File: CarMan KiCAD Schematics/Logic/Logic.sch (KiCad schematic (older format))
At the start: 48 parts, among them J1 Motor Controller Can Line, J2 NON-ISO I2C Testing Header, J3 Logic-TSI Connector, J4 GLV BOB, J5 PIC program, J6 You're Welcome -Ethan, J666 Real Time Clock, U1 MCP9700AT-HTT-Sensor_Temperat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, U10 BNO_055, U3 PIC32MZ2048EFM064-I_PT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

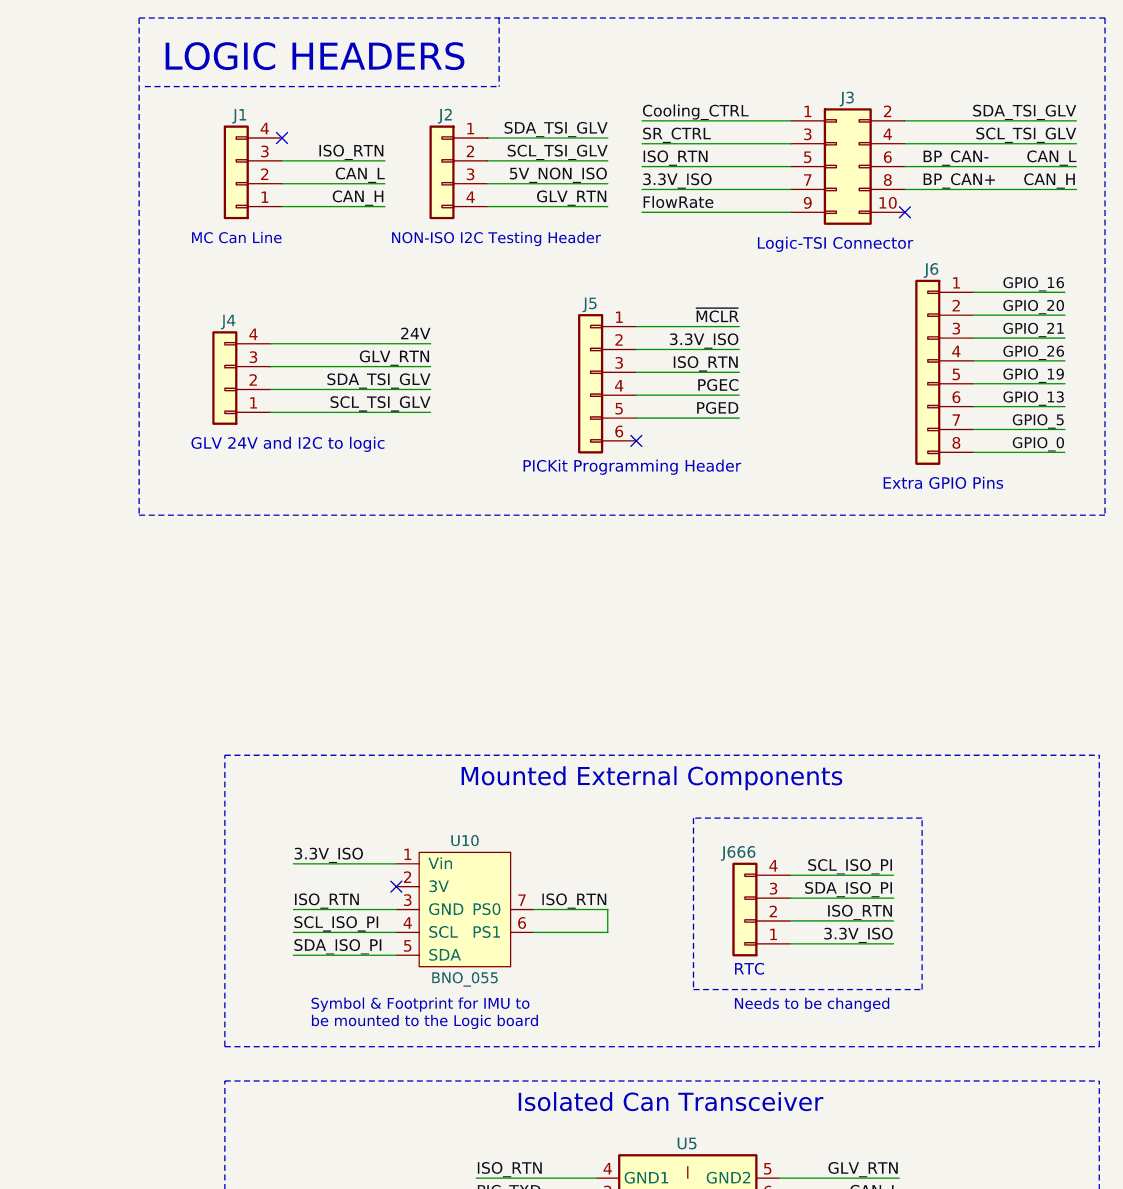
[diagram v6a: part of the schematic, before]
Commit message: Added Footprint for Pi RTC. organized board
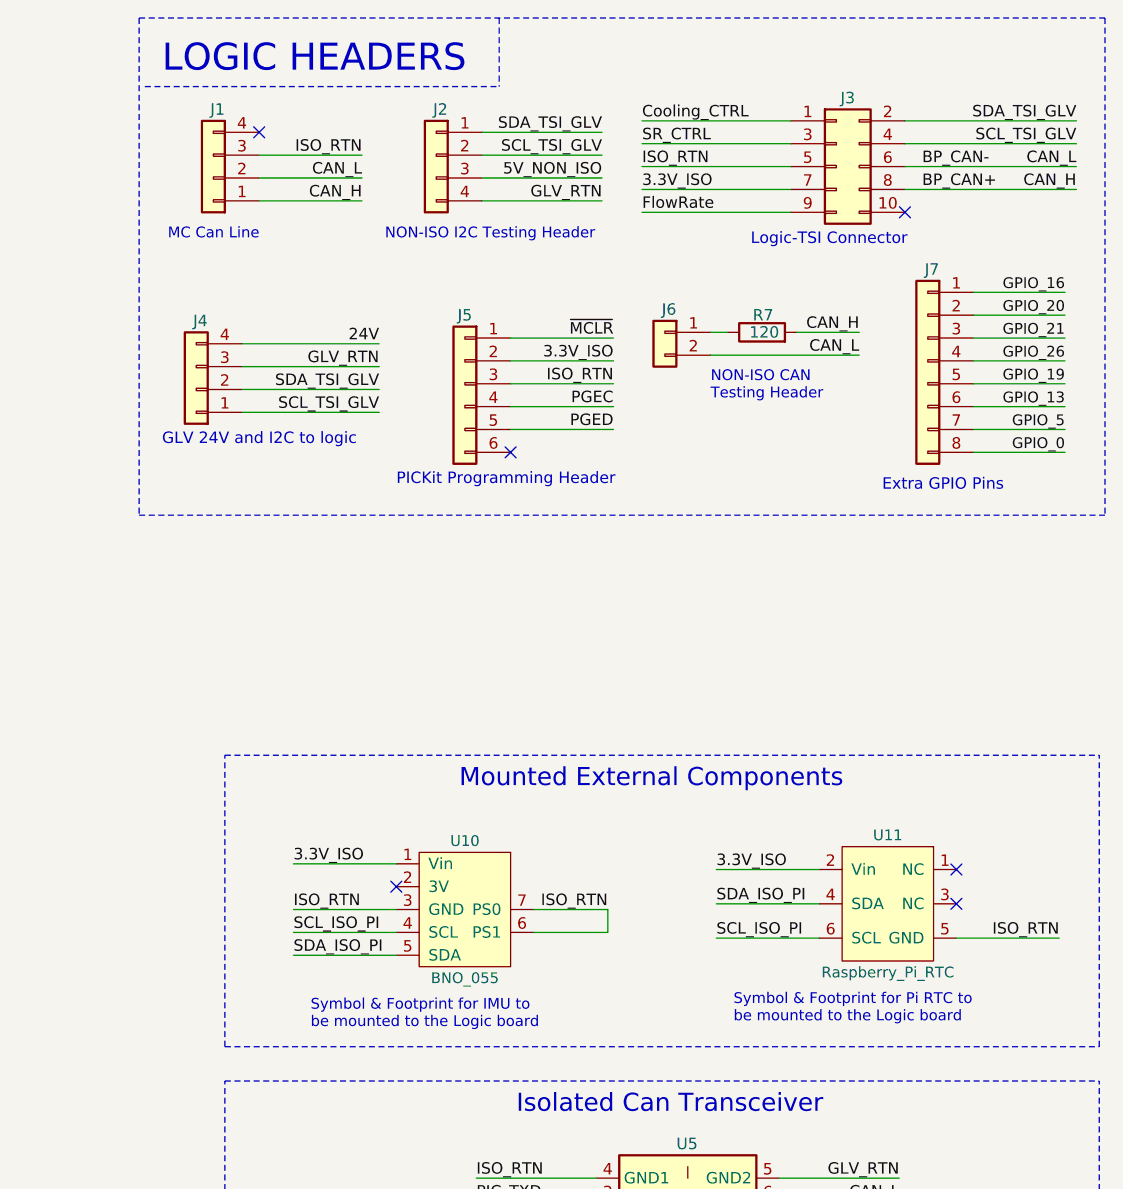
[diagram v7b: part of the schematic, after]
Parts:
- removed J666: Real Time Clock, Connector_PinHeader_2.54mm:PinHeader_1x04_P2.54mm_Vertical, symbol Logic-rescue:Conn_01x04-Connector_Generic-Logic-rescue
- added J6: NON-ISO CAN Testing, Connector_PinSocket_2.54mm:PinSocket_1x02_P2.54mm_Vertical, symbol Connector_Generic:Conn_01x02
- added R7: 120, Resistor_SMD:R_0805_2012Metric_Pad1.15x1.40mm_HandSolder, symbol Logic-rescue:R-Device-Logic-rescue
- added U11: Raspberry_Pi_RTC, CarMan General Footprints:Raspberry_Pi_RTC, symbol CarMan_KiCAD_Library:Raspberry_Pi_RTC
- renumbered J6 to J7
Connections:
- net 3.3V_ISO: now also U11.2 (Vin)
- net BP_CAN+: now also R7.2
- net BP_CAN-: now also J6.2 (Pin_2)
- net ISO_RTN: now also U11.5 (GND)
- net SCL_ISO_PI: now also U11.6 (SCL)
- net SDA_ISO_PI: now also U11.4 (SDA)
- new net: J6.1 (Pin_1), R7.1
- no-connect marks 55 -> 57
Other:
- note added: "NON-ISO CAN\nTesting Header"
- note added: "Symbol & Footprint for Pi RTC to\nbe mounted to the Logic board"
- note removed: "Needs to be changed"
- note removed: "RTC"
- moved on the sheet: J1, J2, J4, J5
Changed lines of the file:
@@
 Comment4 ""
 $EndDescr
-$Comp
-L Logic-rescue:Conn_01x04-Connector_Generic-Logic-rescue J666
-U 1 1 5F95B763
-P 14425 4475
-F 0 "J666" H 14375 4175 50  0000 L CNN
-F 1 "Real Time Clock" H 14350 4700 50  0001 L CNN
-F 2 "Connector_PinHeader_2.54mm:PinHeader_1x04_P2.54mm_Vertical" H 14425 4475 50  0001 C CNN
-F 3 "~" H 14425 4475 50  0001 C CNN
-	1    14425 4475
-	-1   0    0    1
-$EndComp
-Text Label 12850 1350 2    50   ~ 0
+Text Label 12750 1325 2    50   ~ 0
 CAN_H
-NoConn ~ 12400 1050
-Wire Wire Line
-	14625 4475 15075 4475
-Wire Wire Line
-	14625 4575 15075 4575
-Text Label 15075 4275 2    50   ~ 0
+NoConn ~ 12300 1025
+Wire Wire Line
+	15350 4550 15800 4550
+Wire Wire Line
+	14750 4250 14300 4250
+Text Label 14300 4550 0    50   ~ 0
 SCL_ISO_PI
-Text Label 15075 4475 2    50   ~ 0
-ISO_RTN
-Text Label 15075 4575 2    50   ~ 0
+Text Label 15800 4550 2    50   ~ 0
+ISO_RTN
+Text Label 14300 4250 0    50   ~ 0
 3.3V_ISO
-Text Label 15075 4375 2    50   ~ 0
+Text Label 14300 4400 0    50   ~ 0
 SDA_ISO_PI
 Text Label 12450 4525 0    50   ~ 0
@@
 NoConn ~ 8575 9375
 $Comp
-L Logic-rescue:Conn_01x08-Connector_Generic-Logic-rescue J6
+L Logic-rescue:Conn_01x08-Connector_Generic-Logic-rescue J7
 U 1 1 5FA1FE07
 P 15225 2025
-F 0 "J6" H 15175 2425 50  0000 L CNN
+F 0 "J7" H 15175 2425 50  0000 L CNN
 F 1 "You're Welcome -Ethan" H 15305 1926 50  0001 L CNN
 F 2 "Connector_PinSocket_2.54mm:PinSocket_1x08_P2.54mm_Vertical" H 15225 2025 50  0001 C CNN
@@
 	12900 4625 12450 4625
 Wire Wire Line
-	14625 4275 15075 4275
-Wire Wire Line
-	14625 4375 15075 4375
+	14750 4550 14300 4550
+Wire Wire Line
+	14750 4400 14300 4400
 Text Label 7825 8775 0    50   ~ 0
 SCL_ISO_PI
@@
 L Logic-rescue:Conn_01x06-Connector_Generic-Logic-rescue J5
 U 1 1 5FDCB4A9
-P 13750 2075
-F 0 "J5" H 13750 2375 50  0000 C CNN
-F 1 "PIC program" H 13750 1650 50  0001 C CNN
-F 2 "Connector_PinSocket_2.54mm:PinSocket_1x06_P2.54mm_Vertical" H 13750 2075 50  0001 C CNN
-F 3 "~" H 13750 2075 50  0001 C CNN
-	1    13750 2075
+P 13200 2125
+F 0 "J5" H 13200 2425 50  0000 C CNN
+F 1 "PIC program" H 13200 1700 50  0001 C CNN
+F 2 "Connector_PinSocket_2.54mm:PinSocket_1x06_P2.54mm_Vertical" H 13200 2125 50  0001 C CNN
+F 3 "~" H 13200 2125 50  0001 C CNN
+	1    13200 2125
 	-1   0    0    -1
 $EndComp
 Wire Wire Line
-	13950 1875 14400 1875
-Wire Wire Line
-	13950 1975 14400 1975
-Wire Wire Line
-	13950 2075 14400 2075
-Wire Wire Line
-	13950 2175 14400 2175
-Wire Wire Line
-	13950 2275 14400 2275
-NoConn ~ 13950 2375
-Text Label 14400 1975 2    50   ~ 0
+	13400 1925 13850 1925
+Wire Wire Line
+	13400 2025 13850 2025
+Wire Wire Line
+	13400 2125 13850 2125
+Wire Wire Line
+	13400 2225 13850 2225
+Wire Wire Line
+	13400 2325 13850 2325
+NoConn ~ 13400 2425
+Text Label 13850 2025 2    50   ~ 0
 3.3V_ISO
-Text Label 14400 1875 2    50   ~ 0
+Text Label 13850 1925 2    50   ~ 0
 ~MCLR~
-Text Label 14400 2075 2    50   ~ 0
-ISO_RTN
-Text Label 14400 2175 2    50   ~ 0
+Text Label 13850 2125 2    50   ~ 0
+ISO_RTN
+Text Label 13850 2225 2    50   ~ 0
 PGEC
-Text Label 14400 2275 2    50   ~ 0
+Text Label 13850 2325 2    50   ~ 0
 PGED
 Text Label 3550 6775 0    50   ~ 0
@@
 L Logic-rescue:Conn_01x04-Connector_Generic-Logic-rescue J4
 U 1 1 5FB30D0C
-P 12150 2150
-F 0 "J4" H 12100 1850 50  0000 L CNN
-F 1 "GLV BOB" H 11975 2375 50  0001 L CNN
-F 2 "CarMan General Footprints:Molex_MiniFit-JR-5556-04A_2x02x4.20mm_Straight" H 12150 2150 50  0001 C CNN
-F 3 "~" H 12150 2150 50  0001 C CNN
-	1    12150 2150
+P 12025 2150
+F 0 "J4" H 11975 1850 50  0000 L CNN
+F 1 "GLV BOB" H 11850 2375 50  0001 L CNN
+F 2 "CarMan General Footprints:Molex_MiniFit-JR-5556-04A_2x02x4.20mm_Straight" H 12025 2150 50  0001 C CNN
+F 3 "~" H 12025 2150 50  0001 C CNN
+	1    12025 2150
 	-1   0    0    1
 $EndComp
-Text Label 13050 2250 2    50   ~ 0
+Text Label 12825 2250 2    50   ~ 0
 SCL_TSI_GLV
-Text Label 13050 2050 2    50   ~ 0
+Text Label 12825 2050 2    50   ~ 0
 GLV_RTN
-Text Label 13050 1950 2    50   ~ 0
+Text Label 12825 1950 2    50   ~ 0
 24V
 $Comp
@@
 Wire Wire Line
 	1400 10825 2050 10825
-Wire Wire Line
-	12350 2050 13050 2050
 Wire Notes Line
 	4300 9450 2675 9450
@@
 Text Notes 950  9625 0    79   ~ 0
 Isolated Status LEDs
-Text Notes 14475 1550 0    50   ~ 0
+Text Notes 14450 1525 0    50   ~ 0
 Logic-TSI Connector
 Text Label 13825 4425 2    50   ~ 0
@@
 Wire Wire Line
 	12900 4425 12450 4425
-Wire Wire Line
-	12350 2150 13050 2150
-Wire Wire Line
-	12350 1950 13050 1950
-Wire Wire Line
-	12350 2250 13050 2250
 Wire Wire Line
 	5375 6375 6000 6375
@@
 Wire Wire Line
 	3150 8575 3675 8575
-Text Label 13050 2150 2    50   ~ 0
+Text Label 12825 2150 2    50   ~ 0
 SDA_TSI_GLV
 Text Label 15300 9275 2    50   ~ 0
@@
 L Logic-rescue:Conn_01x04-Connector_Generic-Logic-rescue J1
 U 1 1 5F95E453
-P 12200 1250
-F 0 "J1" H 12150 950 50  0000 L CNN
-F 1 "Motor Controller Can Line" H 11625 1450 50  0001 L CNN
-F 2 "CarMan General Footprints:Molex_MiniFit-JR-5556-04A_2x02x4.20mm_Straight" H 12200 1250 50  0001 C CNN
-F 3 "~" H 12200 1250 50  0001 C CNN
-	1    12200 1250
+P 12100 1225
+F 0 "J1" H 12050 925 50  0000 L CNN
+F 1 "Motor Controller Can Line" H 11525 1425 50  0001 L CNN
+F 2 "CarMan General Footprints:Molex_MiniFit-JR-5556-04A_2x02x4.20mm_Straight" H 12100 1225 50  0001 C CNN
+F 3 "~" H 12100 1225 50  0001 C CNN
+	1    12100 1225
 	-1   0    0    1
 $EndComp
-Text Notes 12000 1525 0    47   ~ 0
+Text Notes 11900 1500 0    47   ~ 0
 MC Can Line
-Text Label 12850 1250 2    50   ~ 0
+Text Label 12750 1225 2    50   ~ 0
 CAN_L
 Wire Wire Line
@@
 Text Notes 11875 775  0    118  ~ 0
 LOGIC HEADERS
-Text Notes 12000 2425 0    50   ~ 0
+Text Notes 11875 2400 0    50   ~ 0
 GLV 24V and I2C to logic
 Wire Notes Line
 	11800 825  13350 825
-Text Notes 13450 2525 0    50   ~ 0
+Text Notes 12900 2575 0    50   ~ 0
 PICKit Programming Header
 Text Label 15825 1725 2    47   ~ 0
@@
 Text Notes 15025 2600 0    50   ~ 0
 Extra GPIO Pins
-Text Label 12850 1150 2    50   ~ 0
-ISO_RTN
-Wire Wire Line
-	12850 1150 12400 1150
-Wire Wire Line
-	12400 1250 12850 1250
-Wire Wire Line
-	12400 1350 12850 1350
+Text Label 12750 1125 2    50   ~ 0
+ISO_RTN
+Wire Wire Line
+	12750 1125 12300 1125
+Wire Wire Line
+	12300 1225 12750 1225
+Wire Wire Line
+	12300 1325 12750 1325
 Wire Wire Line
 	13500 4425 13825 4425
@@
 Wire Wire Line
 	7825 10375 8575 10375
-Text Notes 14375 4725 0    50   ~ 0
-RTC
 Wire Wire Line
 	6725 3375 7225 3375
@@
 L Logic-rescue:Conn_01x04-Connector_Generic-Logic-rescue J2
 U 1 1 60721A5C
-P 13100 1150
-F 0 "J2" H 13050 1350 50  0000 L CNN
-F 1 "NON-ISO I2C Testing Header" H 12525 1350 50  0001 L CNN
-F 2 "Connector_PinSocket_2.54mm:PinSocket_1x04_P2.54mm_Vertical" H 13100 1150 50  0001 C CNN
-F 3 "~" H 13100 1150 50  0001 C CNN
-	1    13100 1150
+P 13075 1125
+F 0 "J2" H 13025 1325 50  0000 L CNN
+F 1 "NON-ISO I2C Testing Header" H 12500 1325 50  0001 L CNN
+F 2 "Connector_PinSocket_2.54mm:PinSocket_1x04_P2.54mm_Vertical" H 13075 1125 50  0001 C CNN
+F 3 "~" H 13075 1125 50  0001 C CNN
+	1    13075 1125
 	-1   0    0    -1
 $EndComp
-Text Notes 12875 1525 0    47   ~ 0
+Text Notes 12850 1500 0    47   ~ 0
 NON-ISO I2C Testing Header
-Text Label 13825 1250 2    50   ~ 0
+Text Label 13800 1225 2    50   ~ 0
 5V_NON_ISO
-Text Label 13825 1350 2    50   ~ 0
+Text Label 13800 1325 2    50   ~ 0
 GLV_RTN
 Wire Wire Line
-	13300 1250 13825 1250
-Wire Wire Line
-	13300 1350 13825 1350
-Text Label 13825 1050 2    50   ~ 0
+	13275 1225 13800 1225
+Wire Wire Line
+	13275 1325 13800 1325
+Text Label 13800 1025 2    50   ~ 0
 SDA_TSI_GLV
 Wire Wire Line
-	13300 1050 13825 1050
-Text Label 13825 1150 2    50   ~ 0
+	13275 1025 13800 1025
+Text Label 13800 1125 2    50   ~ 0
 SCL_TSI_GLV
 Wire Wire Line
-	13825 1150 13300 1150
+	13800 1125 13275 1125
 $Comp
 L Device:C C?
@@
 Wire Notes Line
 	11775 2700 16000 2700
-Wire Notes Line
-	14200 4775 15200 4775
-Wire Notes Line
-	15200 4775 15200 4025
-Wire Notes Line
-	15200 4025 14200 4025
-Wire Notes Line
-	14200 4025 14200 4775
-Text Notes 14375 4875 0    47   ~ 0
-Needs to be changed
 Wire Wire Line
 	750  8125 1225 8125
@@
 Wire Wire Line
 	2050 8125 2525 8125
+$Comp
+L CarMan_KiCAD_Library:Raspberry_Pi_RTC U11
+U 1 1 60875061
+P 15050 4400
+F 0 "U11" H 15050 4700 47  0000 C CNN
+F 1 "Raspberry_Pi_RTC" H 15050 4100 47  0000 C CNN
+F 2 "CarMan General Footprints:Raspberry_Pi_RTC" V 15050 4400 47  0001 C CNN
+F 3 "" V 15050 4400 47  0001 C CNN
+	1    15050 4400
+	1    0    0    -1
+$EndComp
+NoConn ~ 15350 4400
+NoConn ~ 15350 4250
+Text Notes 14375 4925 0    47   ~ 0
+Symbol & Footprint for Pi RTC to\nbe mounted to the Logic board
+$Comp
+L Logic-rescue:R-Device-Logic-rescue R7
+U 1 1 6099A2A5
+P 14500 1900
+AR Path="/6099A2A5" Ref="R7"  Part="1"
+AR Path="/5F9A7CF0/6099A2A5" Ref="R?"  Part="1"
+F 0 "R7" V 14575 1850 50  0000 L CNN
+F 1 "120" V 14500 1825 50  0000 L CNN
+F 2 "Resistor_SMD:R_0805_2012Metric_Pad1.15x1.40mm_HandSolder" V 14430 1900 50  0001 C CNN
+F 3 "~" H 14500 1900 50  0001 C CNN
+	1    14500 1900
+	0    -1   -1   0
+$EndComp
+$Comp
+L Connector_Generic:Conn_01x02 J6
+U 1 1 6099A2AB
+P 14075 1900
+AR Path="/6099A2AB" Ref="J6"  Part="1"
+AR Path="/5F9A7CF0/6099A2AB" Ref="J?"  Part="1"
+F 0 "J6" H 14025 2000 50  0000 L CNN
+F 1 "NON-ISO CAN Testing" H 13925 1675 50  0001 L CNN
+F 2 "Connector_PinSocket_2.54mm:PinSocket_1x02_P2.54mm_Vertical" H 14075 1900 50  0001 C CNN
+F 3 "~" H 14075 1900 50  0001 C CNN
+	1    14075 1900
+	-1   0    0    -1
+$EndComp
+Text Notes 14275 2200 0    47   ~ 0
+NON-ISO CAN\nTesting Header
+Wire Wire Line
+	14650 1900 14925 1900
+Text Label 14925 1900 2    50   ~ 0
+CAN_H
+Wire Wire Line
+	14275 2000 14925 2000
+Wire Wire Line
+	14350 1900 14275 1900
+Text Label 14925 2000 2    50   ~ 0
+CAN_L
+Wire Wire Line
+	12225 1950 12825 1950
+Wire Wire Line
+	12825 2050 12225 2050
+Wire Wire Line
+	12225 2150 12825 2150
+Wire Wire Line
+	12825 2250 12225 2250
 $EndSCHEMATC
